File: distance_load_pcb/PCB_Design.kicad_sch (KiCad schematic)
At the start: 16 parts, among them J1 From Power Source 5V, J2 From Limit Switch (LS), J3 From Encoder (EC), J4 From Power Source 15V, J5 Screen_Front, J6 Screen_Back, J7 From Load Cell (LC), U2 YAAJ_BluePill_Part_Like_SWD_B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

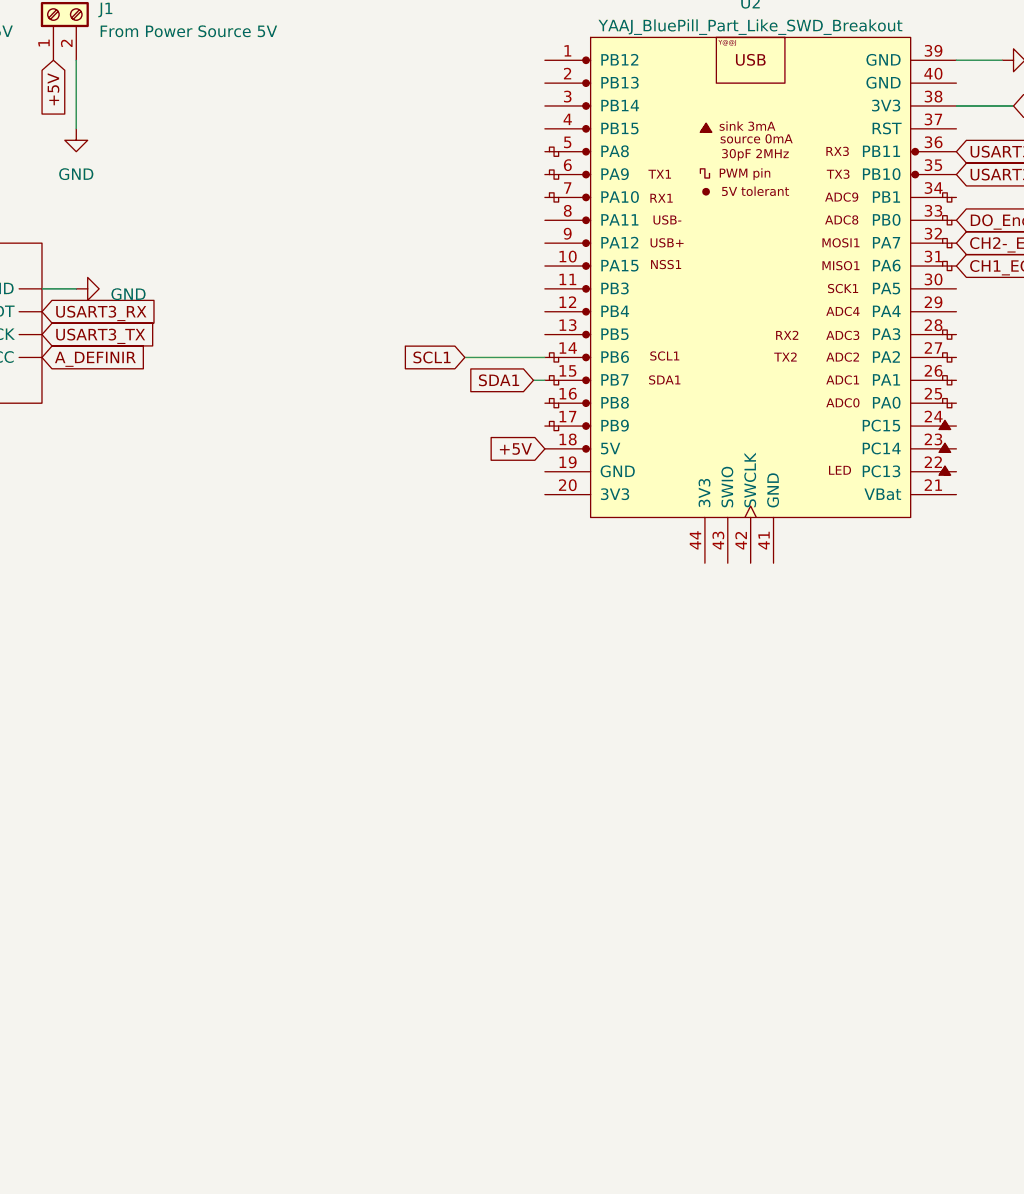
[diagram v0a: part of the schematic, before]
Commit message: separate 3 folders for each pcb
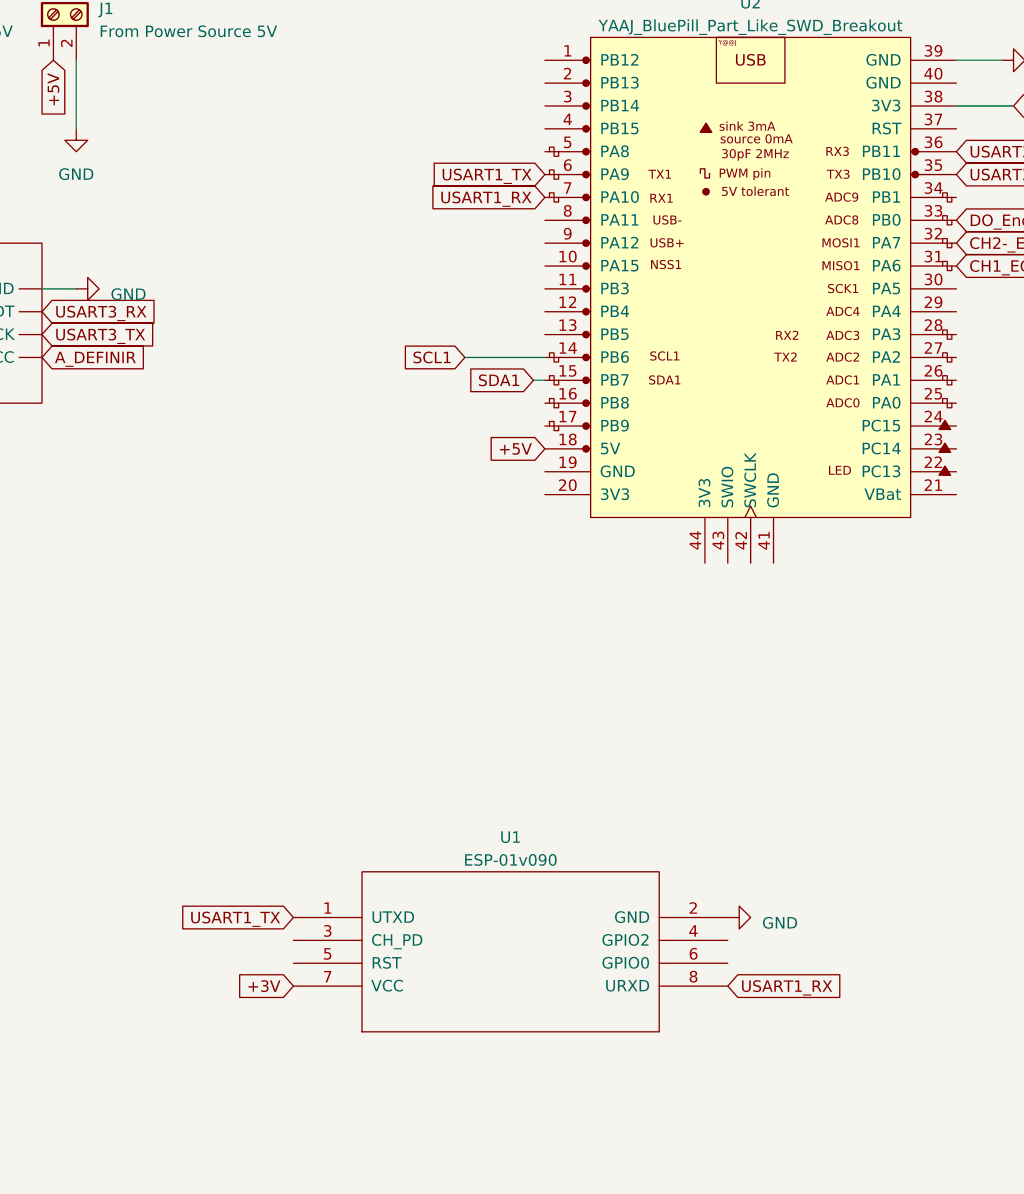
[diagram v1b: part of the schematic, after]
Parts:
- added U1: ESP-01v090, symbol ESP8266:ESP-01v090
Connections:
- net +3V: now also U1.7 (VCC)
- net GND: now also U1.2 (GND)
- net USART1_TX: now reaches U2.6 (PA9)
- net USART1_TX: now also U1.1 (UTXD)
- net USART1_RX: now reaches U2.7 (PA10)
- net USART1_RX: now also U1.8 (URXD)
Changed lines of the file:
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@@
+    )
+  )
+  (global_label "USART1_RX" (shape input) (at 238.76 132.08 0) (fields_autoplaced)
+    (effects (font (size 1.27 1.27)) (justify left))
+    (property "Intersheetrefs" "${INTERSHEET_REFS}" (at 252.1886 132.08 0)
+      (effects (font (size 1.27 1.27)) (justify left) hide)
     )
   )
@@
     )
   )
+  (global_label "USART1_RX" (shape input) (at 218.44 44.45 180) (fields_autoplaced)
+    (effects (font (size 1.27 1.27)) (justify right))
+    (property "Intersheetrefs" "${INTERSHEET_REFS}" (at 205.0114 44.45 0)
+      (effects (font (size 1.27 1.27)) (justify right) hide)
+    )
+  )
+  (global_label "USART1_TX" (shape input) (at 218.44 41.91 180) (fields_autoplaced)
+    (effects (font (size 1.27 1.27)) (justify right))
+    (property "Intersheetrefs" "${INTERSHEET_REFS}" (at 205.3138 41.91 0)
+      (effects (font (size 1.27 1.27)) (justify right) hide)
+    )
+  )
   (global_label "V+_EC" (shape input) (at 106.68 142.24 0) (fields_autoplaced)
     (effects (font (size 1.27 1.27)) (justify left))
@@
     )
   )
+  (global_label "+3V" (shape input) (at 190.5 132.08 180) (fields_autoplaced)
+    (effects (font (size 1.27 1.27)) (justify right))
+    (property "Intersheetrefs" "${INTERSHEET_REFS}" (at 183.7237 132.08 0)
+      (effects (font (size 1.27 1.27)) (justify right) hide)
+    )
+  )
   (global_label "CH1_EC" (shape input) (at 264.16 52.07 0) (fields_autoplaced)
     (effects (font (size 1.27 1.27)) (justify left))
@@
     (effects (font (size 1.27 1.27)) (justify right))
     (property "Intersheetrefs" "${INTERSHEET_REFS}" (at 82.3656 52.07 0)
+      (effects (font (size 1.27 1.27)) (justify right) hide)
+    )
+  )
+  (global_label "USART1_TX" (shape input) (at 190.5 124.46 180) (fields_autoplaced)
+    (effects (font (size 1.27 1.27)) (justify right))
+    (property "Intersheetrefs" "${INTERSHEET_REFS}" (at 177.3738 124.46 0)
       (effects (font (size 1.27 1.27)) (justify right) hide)
     )
@@
     )
   )
+  (symbol (lib_id "power:GND") (at 238.76 124.46 90) (unit 1)
+    (in_bom yes) (on_board yes) (dnp no) (fields_autoplaced)
+    (property "Reference" "#PWR05" (at 245.11 124.46 0)
+      (effects (font (size 1.27 1.27)) hide)
+    )
+    (property "Value" "GND" (at 242.57 125.095 90)
+      (effects (font (size 1.27 1.27)) (justify right))
+    )
+    (property "Footprint" "" (at 238.76 124.46 0)
+      (effects (font (size 1.27 1.27)) hide)
+    )
+    (property "Datasheet" "" (at 238.76 124.46 0)
+      (effects (font (size 1.27 1.27)) hide)
+    )
+    (pin "1")
+    (instances
+      (project "PCB_Design"
+        (path "/8cc55c57-4762-4316-b75d-1232f5681ca6"
+          (reference "#PWR05") (unit 1)
+        )
+      )
+    )
+  )
   (symbol (lib_id "Device:R") (at 48.26 36.83 0) (unit 1)
     (in_bom yes) (on_board yes) (dnp no) (fields_autoplaced)
@@
         )
       )
+    )
+  )
+  (symbol (lib_id "ESP8266:ESP-01v090") (at 214.63 128.27 0) (unit 1)
+    (in_bom yes) (on_board yes) (dnp no) (fields_autoplaced)
+    (property "Reference" "U1" (at 214.63 115.57 0)
+      (effects (font (size 1.27 1.27)))
+    )
+    (property "Value" "ESP-01v090" (at 214.63 118.11 0)
+      (effects (font (size 1.27 1.27)))
+    )
+    (property "Footprint" "" (at 214.63 128.27 0)
+      (effects (font (size 1.27 1.27)) hide)
+    )
+    (property "Datasheet" "http://l0l.org.uk/2014/12/esp8266-modules-hardware-guide-gotta-catch-em-all/" (at 214.63 128.27 0)
+      (effects (font (size 1.27 1.27)) hide)
+    )
+    (pin "1")
+    (pin "2")
+    (pin "3")
+    (pin "4")
+    (pin "5")
+    (pin "6")
+    (pin "7")
+    (pin "8")
+    (instances
+      (project "PCB_Design"
+        (path "/8cc55c57-4762-4316-b75d-1232f5681ca6"
+          (reference "U1") (unit 1)
+        )
+      )

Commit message: add PCB footprint force and distance module[D
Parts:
- J1: footprint (none) -> TerminalBlock_TE-Connectivity:TerminalBlock_TE_282834-2_1x02_P2.54mm_Horizontal
- J2, J4, JP1, JP2: footprint (none) -> Connector_PinHeader_2.54mm:PinHeader_1x02_P2.54mm_Vertical
- J3, J7: footprint (none) -> Connector_PinHeader_2.54mm:PinHeader_1x05_P2.54mm_Vertical
- J5, J6: footprint (none) -> Connector_PinHeader_2.54mm:PinHeader_1x04_P2.54mm_Vertical
- R1, R2, R5, R6, R7: footprint (none) -> Resistor_THT:R_Axial_DIN0207_L6.3mm_D2.5mm_P10.16mm_Horizontal
- U1: footprint (none) -> ESP8266:ESP-01
- U2: footprint (none) -> Footprints:YAAJ_BluePill_SWD_1
- U3: footprint (none) -> HX711:HX711
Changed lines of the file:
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@@
       (effects (font (size 1.27 1.27)))
     )
-    (property "Footprint" "" (at 34.29 54.61 0)
+    (property "Footprint" "Connector_PinHeader_2.54mm:PinHeader_1x04_P2.54mm_Vertical" (at 34.29 54.61 0)
       (effects (font (size 1.27 1.27)) hide)
     )
@@
       (effects (font (size 1.27 1.27)))
     )
-    (property "Footprint" "" (at 94.742 111.76 90)
+    (property "Footprint" "Resistor_THT:R_Axial_DIN0207_L6.3mm_D2.5mm_P10.16mm_Horizontal" (at 94.742 111.76 90)
       (effects (font (size 1.27 1.27)) hide)
     )
@@
       (effects (font (size 1.27 1.27)) (justify left))
     )
-    (property "Footprint" "" (at 46.482 72.39 90)
+    (property "Footprint" "Resistor_THT:R_Axial_DIN0207_L6.3mm_D2.5mm_P10.16mm_Horizontal" (at 46.482 72.39 90)
       (effects (font (size 1.27 1.27)) hide)
     )
@@
       (effects (font (size 1.27 1.27)))
     )
-    (property "Footprint" "" (at 96.52 88.9 0)
+    (property "Footprint" "Connector_PinHeader_2.54mm:PinHeader_1x02_P2.54mm_Vertical" (at 96.52 88.9 0)
       (effects (font (size 1.27 1.27)) hide)
     )
@@
       (effects (font (size 1.27 1.27)))
     )
-    (property "Footprint" "" (at 96.52 69.85 0)
+    (property "Footprint" "Connector_PinHeader_2.54mm:PinHeader_1x02_P2.54mm_Vertical" (at 96.52 69.85 0)
       (effects (font (size 1.27 1.27)) hide)
     )
@@
       (effects (font (size 1.27 1.27)) (justify right))
     )
-    (property "Footprint" "" (at 163.83 24.13 0)
+    (property "Footprint" "TerminalBlock_TE-Connectivity:TerminalBlock_TE_282834-2_1x02_P2.54mm_Horizontal" (at 163.83 24.13 0)
       (effects (font (size 1.27 1.27)) hide)
     )
@@
       (effects (font (size 1.27 1.27)) (justify right))
     )
-    (property "Footprint" "" (at 41.402 39.37 90)
+    (property "Footprint" "Resistor_THT:R_Axial_DIN0207_L6.3mm_D2.5mm_P10.16mm_Horizontal" (at 41.402 39.37 90)
       (effects (font (size 1.27 1.27)) hide)
     )
@@
       (effects (font (size 1.27 1.27)) (justify left))
     )
-    (property "Footprint" "" (at 46.482 36.83 90)
+    (property "Footprint" "Resistor_THT:R_Axial_DIN0207_L6.3mm_D2.5mm_P10.16mm_Horizontal" (at 46.482 36.83 90)
       (effects (font (size 1.27 1.27)) hide)
     )
@@
       (effects (font (size 1.27 1.27)) (justify left))
     )
-    (property "Footprint" "" (at 100.33 137.16 0)
+    (property "Footprint" "Connector_PinHeader_2.54mm:PinHeader_1x05_P2.54mm_Vertical" (at 100.33 137.16 0)
       (effects (font (size 1.27 1.27)) hide)
     )
@@
       (effects (font (size 1.27 1.27)))
     )
-    (property "Footprint" "" (at 96.52 52.07 0)
+    (property "Footprint" "Connector_PinHeader_2.54mm:PinHeader_1x02_P2.54mm_Vertical" (at 96.52 52.07 0)
       (effects (font (size 1.27 1.27)) hide)
     )
@@
       (effects (font (size 1.27 1.27)))
     )
-    (property "Footprint" "" (at 214.63 128.27 0)
+    (property "Footprint" "ESP8266:ESP-01" (at 214.63 128.27 0)
       (effects (font (size 1.27 1.27)) hide)
     )
@@
       (effects (font (size 1.27 1.27)) (justify right))
     )
-    (property "Footprint" "" (at 133.35 24.13 0)
+    (property "Footprint" "Connector_PinHeader_2.54mm:PinHeader_1x02_P2.54mm_Vertical" (at 133.35 24.13 0)
       (effects (font (size 1.27 1.27)) hide)
     )
@@
       (effects (font (size 1.27 1.27)) (justify left))
     )
-    (property "Footprint" "" (at 96.52 24.13 0)
+    (property "Footprint" "Connector_PinHeader_2.54mm:PinHeader_1x05_P2.54mm_Vertical" (at 96.52 24.13 0)
       (effects (font (size 1.27 1.27)) hide)
     )
@@
       (effects (font (size 1.27 1.27)) (justify right))
     )
-    (property "Footprint" "" (at 41.402 74.93 90)
+    (property "Footprint" "Resistor_THT:R_Axial_DIN0207_L6.3mm_D2.5mm_P10.16mm_Horizontal" (at 41.402 74.93 90)
       (effects (font (size 1.27 1.27)) hide)
     )
@@
       (effects (font (size 1.27 1.27)))
     )
-    (property "Footprint" "" (at 261.62 77.47 0)
+    (property "Footprint" "Footprints:YAAJ_BluePill_SWD_1" (at 261.62 77.47 0)
       (effects (font (size 1.27 1.27)) hide)
     )
@@
       (effects (font (size 1.27 1.27)))
     )
-    (property "Footprint" "" (at 143.51 63.5 0)
+    (property "Footprint" "HX711:HX711" (at 143.51 63.5 0)
       (effects (font (size 1.27 1.27)) hide)
     )
@@
       (effects (font (size 1.27 1.27)))
     )
-    (property "Footprint" "" (at 34.29 90.17 0)
-      (effects (font (size 1.27 1.27)) hide)
-    )
+    (property "Footprint" "Connector_PinHeader_2.54mm:PinHeader_1x04_P2.54mm_Vertical" (at 34.29 90.17 0)
+      (effects (font (size 1.27 1.27)) hide)
+    )

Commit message: Fixed problems, working on footprint tracks and pads
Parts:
- removed J4: From Power Source 15V, Connector_PinHeader_2.54mm:PinHeader_1x02_P2.54mm_Vertical, symbol Connector:Screw_Terminal_01x02
- removed R6, R7: 4.7k, Resistor_THT:R_Axial_DIN0207_L6.3mm_D2.5mm_P10.16mm_Horizontal, symbol Device:R
- removed U3: ~, HX711:HX711, symbol New_Library:HX711_Board
- added U4: ~, HX711:HX711, symbol New_Library:HX711_Board
- JP1, JP2: footprint Connector_PinHeader_2.54mm:PinHeader_1x02_P2.54mm_Vertical -> Connector_PinHeader_2.54mm:PinHeader_1x03_P2.54mm_Vertical
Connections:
- net A+: now also U4.A-
- net A-: now also U4.A+
- net A_DEFINIR: now also U4.VCC
- net B+: now also U4.B-
- net B-: now also U4.B+
- net GND: now also U4.E-, U4.GND
- net SDA1: now also R1.2; no longer R1.1
- net USART3_RX: now also U4.DT
- net USART3_TX: now also U4.SCK
- net V+_LC: now also U4.E+
- net +3V renamed +3.3V
- net +3.3V: now also R1.1; no longer R1.2

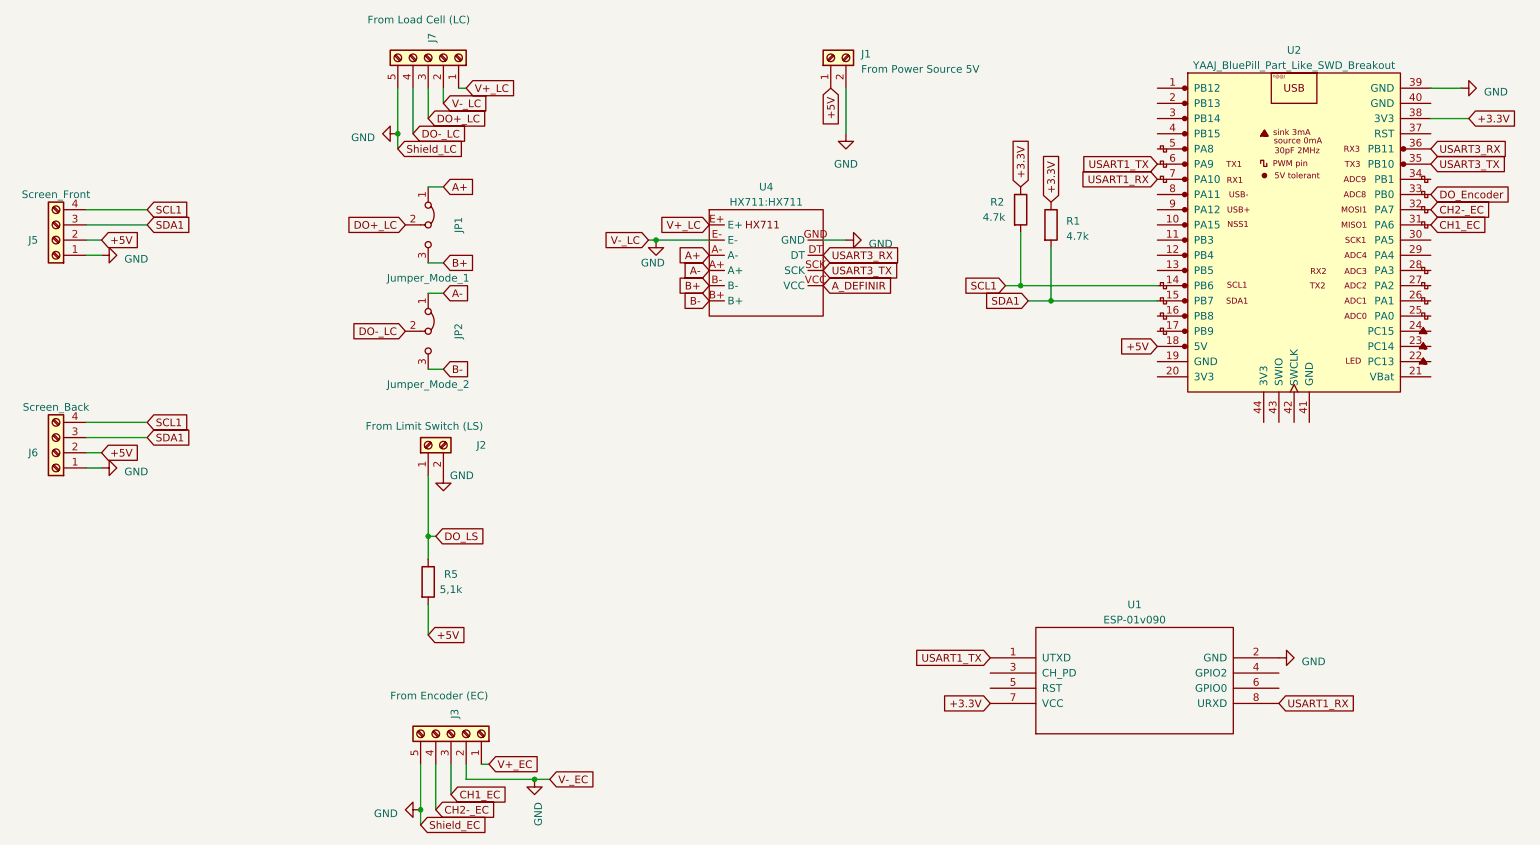
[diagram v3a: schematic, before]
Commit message: finish pcb force and distance
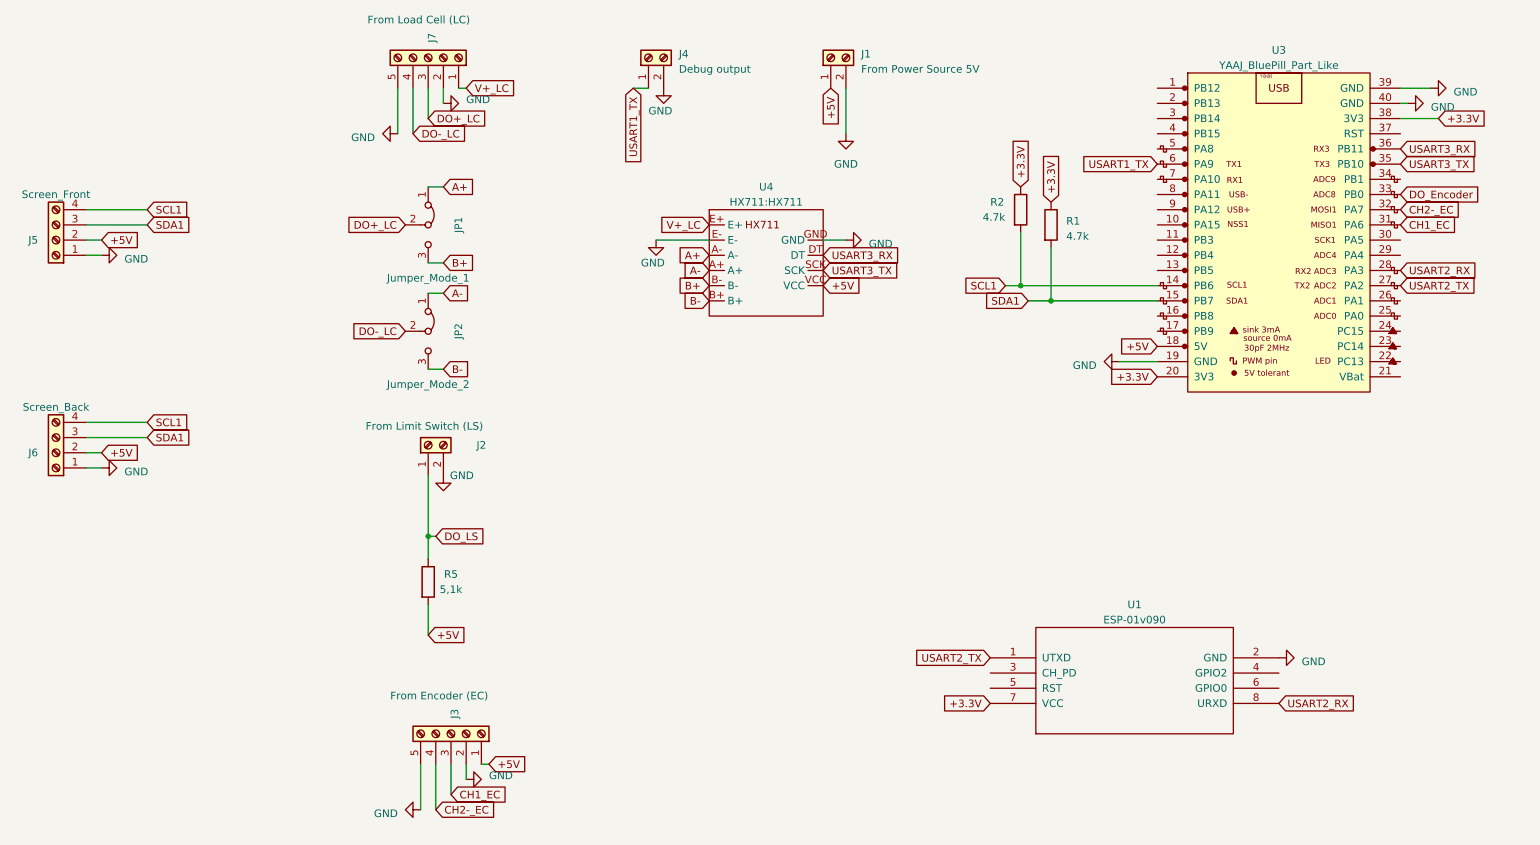
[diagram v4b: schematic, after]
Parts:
- removed U2: YAAJ_BluePill_Part_Like_SWD_Breakout, Footprints:YAAJ_BluePill_SWD_1, symbol YAAJ_BluePill_Part_Like_SWD_Breakout:YAAJ_BluePill_Part_Like_SWD_Breakout
- added J4: Debug output, TerminalBlock_TE-Connectivity:TerminalBlock_TE_282834-2_1x02_P2.54mm_Horizontal, symbol Connector:Screw_Terminal_01x02
- added U3: YAAJ_BluePill_Part_Like, Footprints:YAAJ_BluePill_1, symbol YAAJ_BluePill_Part_Like:YAAJ_BluePill_Part_Like
- J2: footprint Connector_PinHeader_2.54mm:PinHeader_1x02_P2.54mm_Vertical -> TerminalBlock_TE-Connectivity:TerminalBlock_TE_282834-2_1x02_P2.54mm_Horizontal
- J3, J7: footprint Connector_PinHeader_2.54mm:PinHeader_1x05_P2.54mm_Vertical -> TerminalBlock_TE-Connectivity:TerminalBlock_TE_282834-5_1x05_P2.54mm_Horizontal
- J5, J6: footprint Connector_PinHeader_2.54mm:PinHeader_1x04_P2.54mm_Vertical -> TerminalBlock_TE-Connectivity:TerminalBlock_TE_282834-4_1x04_P2.54mm_Horizontal
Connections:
- net A_DEFINIR is gone; now on net +5V: U4.VCC
- net V+_EC is gone; now on net +5V: J3.1 (Pin_1)
- net +3.3V: now also U3.20 (3V3), U3.38 (3V3)
- net +5V: now also U3.18 (5V)
- net CH1_EC: now also U3.31 (PA6)
- net CH2-_EC: now also U3.32 (PA7)
- net DO_Encoder: now also U3.33 (PB0)
- net GND: now also J4.2 (Pin_2), U3.19 (GND), U3.39 (GND), U3.40 (GND)
- net SCL1: now also U3.14 (PB6)
- net SDA1: now also U3.15 (PB7)
- net USART1_TX: now also J4.1 (Pin_1), U3.6 (PA9); no longer U1.1 (UTXD)
- net USART3_RX: now also U3.36 (PB11)
- net USART3_TX: now also U3.35 (PB10)
- net USART1_RX renamed USART2_RX
- net USART2_RX: now also U3.28 (PA3)
- new net USART2_TX: U1.1 (UTXD), U3.27 (PA2)
